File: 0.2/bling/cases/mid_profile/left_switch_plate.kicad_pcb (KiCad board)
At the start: 2 copper layers, 113.3 x 99.7 mm, 1 part

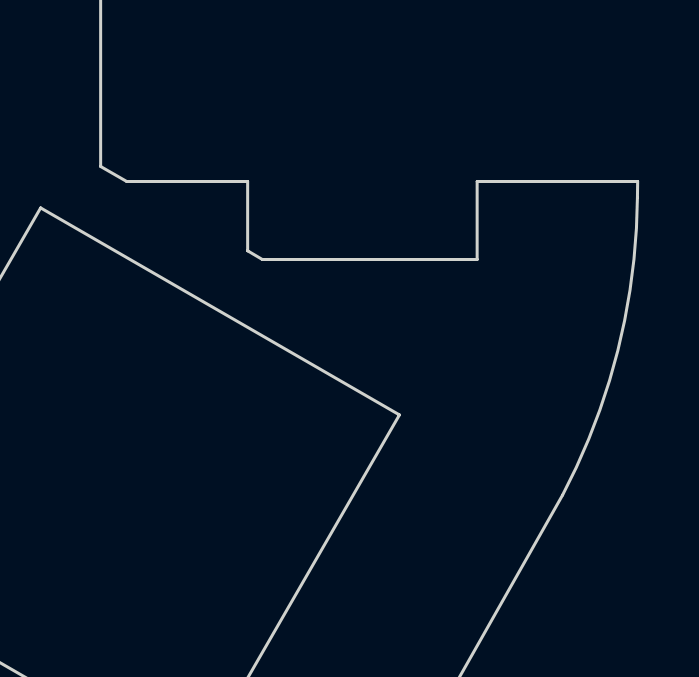
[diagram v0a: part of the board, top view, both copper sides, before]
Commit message: Bling case: make more space for the TRRS connector
I had to manually trim this bit up on my prototype batch. It interferes
with the Jack cable.
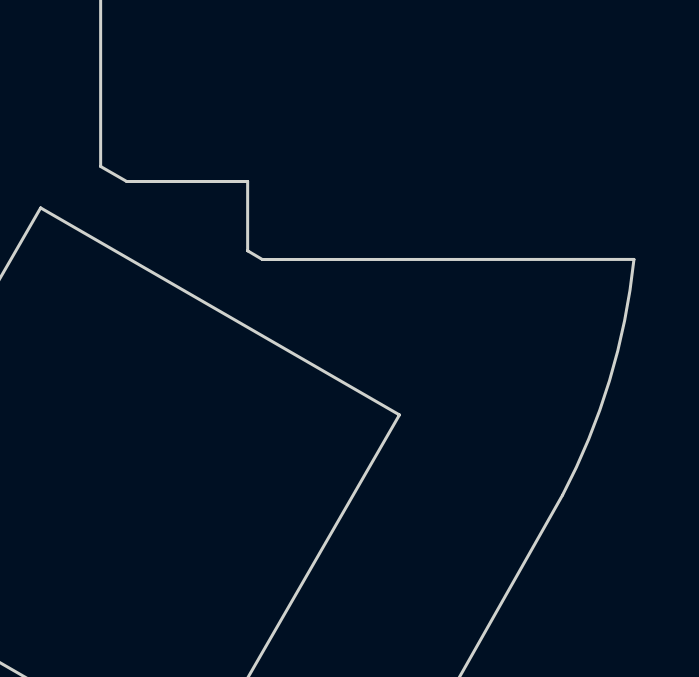
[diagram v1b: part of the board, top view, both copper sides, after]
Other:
- board size 113.3 x 99.7 mm -> 113.2 x 99.7 mm
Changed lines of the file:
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@@
-(kicad_pcb (version 20171130) (host pcbnew 5.1.9)
+(kicad_pcb (version 20171130) (host pcbnew 5.1.10)
   (general
     (thickness 1.6)
-    (drawings 137)
+    (drawings 134)
     (tracks 0)
     (zones 0)
@@
   (gr_arc (start 101.403543 18.190204) (end 106.153543 18.190204) (angle -70.11765915) (layer Edge.Cuts) (width 0.1))
   (gr_arc (start 51.931484 152.624677) (end 103.018969 13.723337) (angle -15.43081601) (layer Edge.Cuts) (width 0.1))
-  (gr_line (start 121.9 79.1) (end 121.893314 79.630452) (layer Edge.Cuts) (width 0.1))
-  (gr_arc (start 100.190263 79.447367) (end 119.398792 89.551246) (angle -27.26148989) (layer Edge.Cuts) (width 0.1))
+  (gr_arc (start 100.190263 79.447367) (end 119.398792 89.551246) (angle -21.79371167) (layer Edge.Cuts) (width 0.1))
   (gr_line (start 119.398792 89.551246) (end 112.550487 101.641178) (layer Edge.Cuts) (width 0.1))
   (gr_arc (start 106.708 97.938735) (end 103.2 103.9) (angle -88.11250382) (layer Edge.Cuts) (width 0.1))
@@
   (gr_line (start 81.09 73.25) (end 94.42 76.82) (layer Edge.Cuts) (width 0.1))
   (gr_line (start 77.52 86.58) (end 81.09 73.25) (layer Edge.Cuts) (width 0.1))
-  (gr_line (start 116.55 81.7) (end 109.39 81.7) (layer Edge.Cuts) (width 0.1))
-  (gr_line (start 116.55 79.1) (end 116.55 81.7) (layer Edge.Cuts) (width 0.1))
-  (gr_line (start 121.9 79.1) (end 116.55 79.1) (layer Edge.Cuts) (width 0.1))
+  (gr_line (start 121.777119 81.697615) (end 109.39 81.7) (layer Edge.Cuts) (width 0.1))
   (gr_line (start 108.9 81.41) (end 108.9 79.1) (layer Edge.Cuts) (width 0.1))
   (gr_line (start 55.35 71.35) (end 55.35 81.65) (layer Edge.Cuts) (width 0.1))
